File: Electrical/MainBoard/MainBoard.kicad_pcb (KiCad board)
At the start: 4 copper layers, 100 x 86.3 mm, 137 parts, among them J1 SNAP Program, J13 Refl_PCB_Connect, J14 Refl_PCB_Connect, J15 Refl_PCB_Connect, J16 Conn_02x03_Odd_Even, J17 MEM2061-01-188-00-A, J18 Conn_02x02_Odd_Even, J19 Conn_02x03_Odd_Even, J2 3.3V Supply, J20 Conn_01x06, J21 Conn_02x03_Odd_Even, J22 Conn_02x02_Odd_Even, J23 Conn_02x03_Odd_Even, J24 Conn_01x04, J25 Conn_02x02_Odd_Even, J26 Conn_02x04_Odd_Even, J3 5V Supply, J4 USB_B_Micro, J5 Battery1, J6 Battery1, J7 GPIO1, J8 Conn_02x04_Odd_Even, J9 USB_B_Micro, SW1 Reset, SW10 SW_SPST, SW2 5V Bypass, SW3 All Power Switch, SW4 User_Button, SW5 User_Button, SW6 User_Button, SW7 SW_SPST, SW8 SW_SPST, SW9 SW_SPST, U1 PIC32MZ2048EFH144-I/PL, U10 DRV8842PWPR, U11 Quad_Encoder_Motor, U12 Quad_Encoder_Motor, U13 DRV8842PWPR, U15 M95M01-DFMN6TP, U2 AP2114HA-3.3TRG1, U3 AP2114HA-3.3TRG1, U5 GSF7002DW, U6 GSF7002DW, U7 GSF7002DW, U8 GSF7002DW, U9 MCP2221A-I_SL

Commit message: Finalize main board and bom
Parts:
- moved C28 6.23 mm to (256.9, 128.2)
- moved U11 6.23 mm to (261.8, 121.8)
- moved U9 5.60 mm to (258.2, 109.3)
- moved C19 5.60 mm to (260.1, 115.0)
- moved D10 5.60 mm to (264.4, 114.1)
- moved D9 5.60 mm to (264.4, 107.6)
- moved J9 5.60 mm to (263.9, 100.0)
- moved R15 5.60 mm to (256.4, 97.0)
- moved R16 5.60 mm to (256.4, 99.1)
- moved J5 0.11 mm to (250.0, 101.0)
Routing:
- net Vdrive: track 208.4 -> 199.3 mm
- net Net-(U11-M-): track 18.3 -> 12.2 mm
- net Net-(U11-M+): track 21.5 -> 16.1 mm
- net /IC2: track 43.6 -> 41.1 mm
- net /IC1: track 39.5 -> 37.1 mm
- net /U1TX: track 49.4 -> 47.0 mm
- net /USB_RST: track 53.7 -> 51.3 mm
- net /U1RX: track 56.7 -> 56.0 mm
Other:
- board text added: "NiMH Batt."

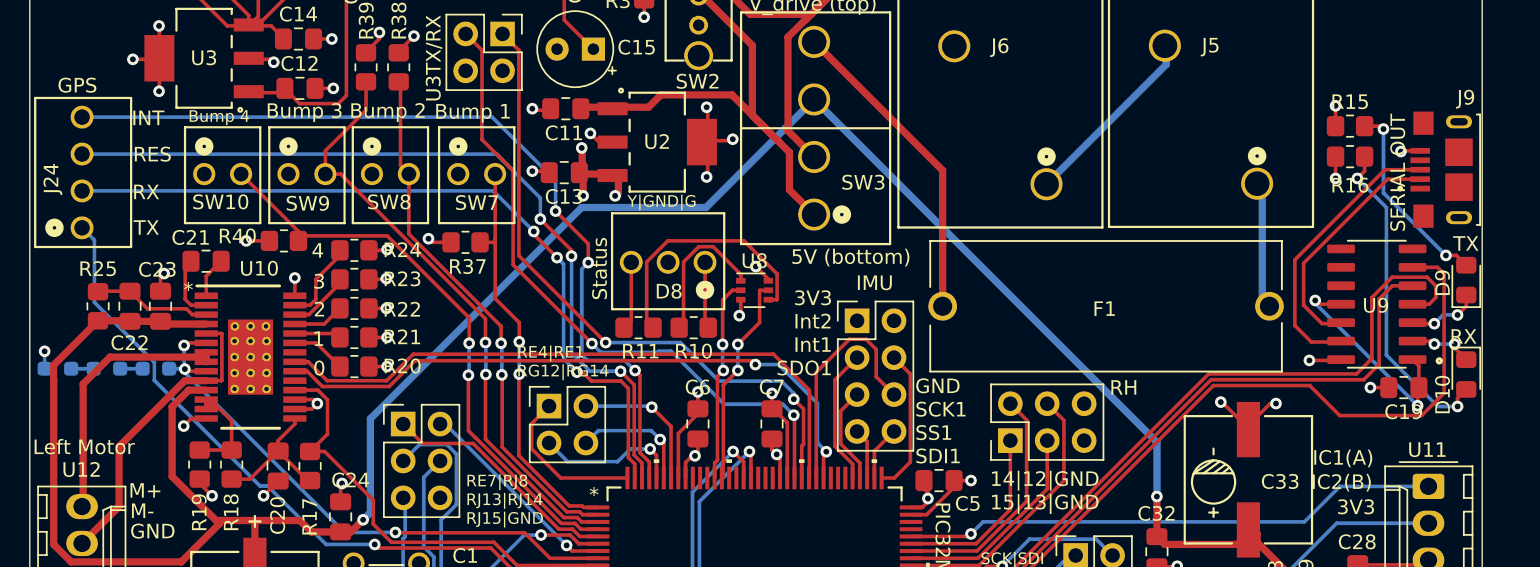
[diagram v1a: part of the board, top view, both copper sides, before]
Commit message: Update the status LED to common anode
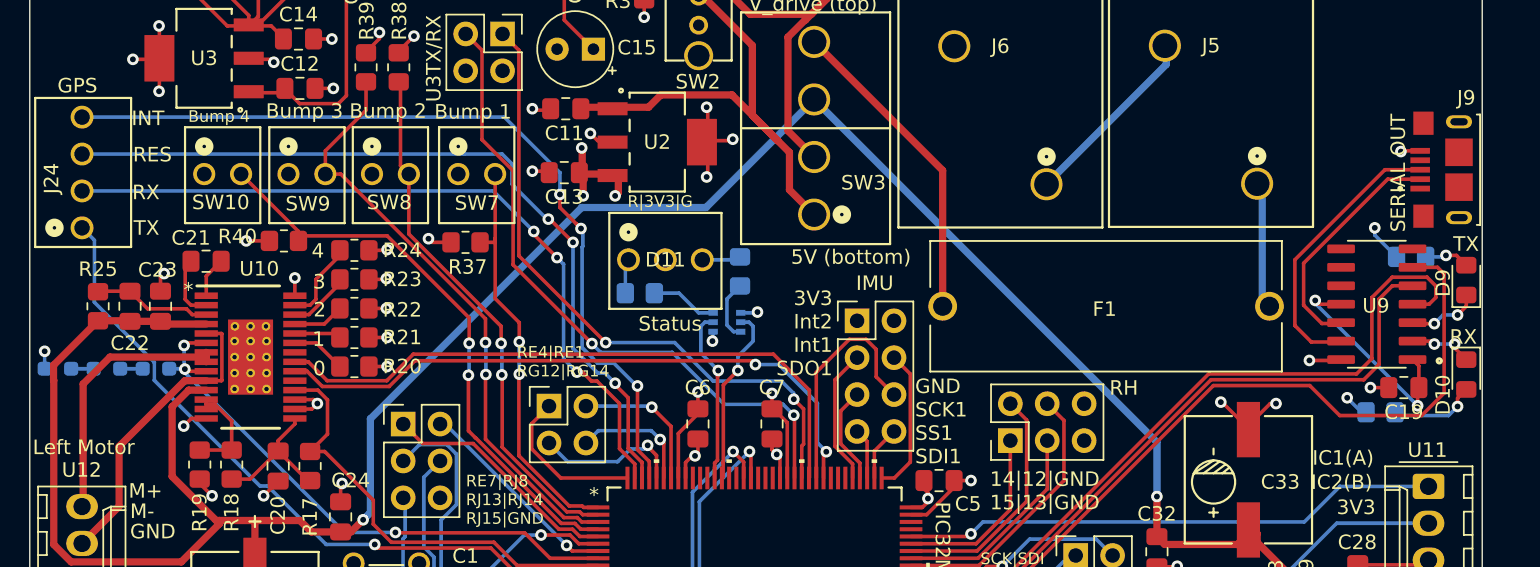
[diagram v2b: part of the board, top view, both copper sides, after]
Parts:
- removed D8: Status_LED, RobotLibrary:CONN3_22232031_MOL
- added D11: Status_LED, RobotLibrary:CONN3_22232031_MOL, F.Cu at (206.7, 106.2)
- R10, R11, R15, R16, U8: moved to B.Cu
- moved R16 17.7 mm to (258.5, 116.7)
- moved R15 9.93 mm to (260.6, 106.0)
- moved R10 5.02 mm to (214.4, 107.0), turned to 90 degrees
- moved U8 2.91 mm to (213.5, 110.5)
- moved R11 2.38 mm to (207.5, 108.5), turned to 180 degrees
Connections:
- R10 pad 1: Net-(D8-A1) -> Net-(U8-D1)
- R10 pad 2: Net-(U8-S1) -> Net-(D11-K2)
- R11 pad 1: Net-(D8-A2) -> Net-(U8-D2)
- R11 pad 2: Net-(U8-S2) -> Net-(D11-K1)
- U8 pad 1: Net-(U8-S1) -> GND
- U8 pad 3: +3.3V -> Net-(U8-D2)
- U8 pad 4: Net-(U8-S2) -> GND
- U8 pad 6: +3.3V -> Net-(U8-D1)
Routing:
- net Net-(U8-S2): track 17.0 -> 0.00 mm
- net Net-(D10-A): track 22.5 -> 6.08 mm, vias 2 -> 1
- net Net-(D9-A): track 13.5 -> 3.12 mm, vias 2 -> 1
- net Net-(U8-S1): track 9.83 -> 0.00 mm
- net Net-(D8-A2): track 4.71 -> 0.00 mm
- net Net-(U8-D2): track 0.00 -> 4.61 mm
- net Net-(D8-A1): track 4.28 -> 0.00 mm
- net Net-(U8-D1): track 0.00 -> 4.04 mm
- net Net-(D11-K2): track 0.00 -> 3.65 mm
- net Net-(D11-K1): track 0.00 -> 2.83 mm
- net /Status_Yellow: track 14.6 -> 12.3 mm, vias 2 -> 1
- net /Status_Green: track 14.0 -> 12.2 mm, vias 2 -> 1
- net GND: track 138.2 -> 140.1 mm, vias 66 -> 68
- net +3.3V: track 148.3 -> 147.3 mm, vias 40 -> 38
- net /U2RX: track 53.5 -> 52.6 mm
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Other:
- board text added: "R|3V3|G"
- board text removed: "Y|GND|G"

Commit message: Finalize the PCBs
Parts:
- moved C24 1.10 mm to (186.9, 122.8)
- moved C1 0.65 mm to (196.1, 128.2)
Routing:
- net /USB_RST: track 51.3 -> 45.0 mm, vias 0 -> 2
- net Net-(D10-K): track 4.39 -> 5.30 mm
- net /Fault1: track 30.6 -> 31.5 mm
- net Vdrive: track 199.3 -> 198.5 mm
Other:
- board text added: "Matthew Sato, 06/11/2025 Engineering Informatics Group Stanford University Robot Control Board, Rev 0.3 Schematic Details: https://github.com/satomm1/Robot"
- board text removed: "Matthew Sato, 05/18/2025 Engineering Informatics Group Stanford University Robot Control Board, Rev 0.3 Schematic Details: https://github.com/satomm1/Robot"

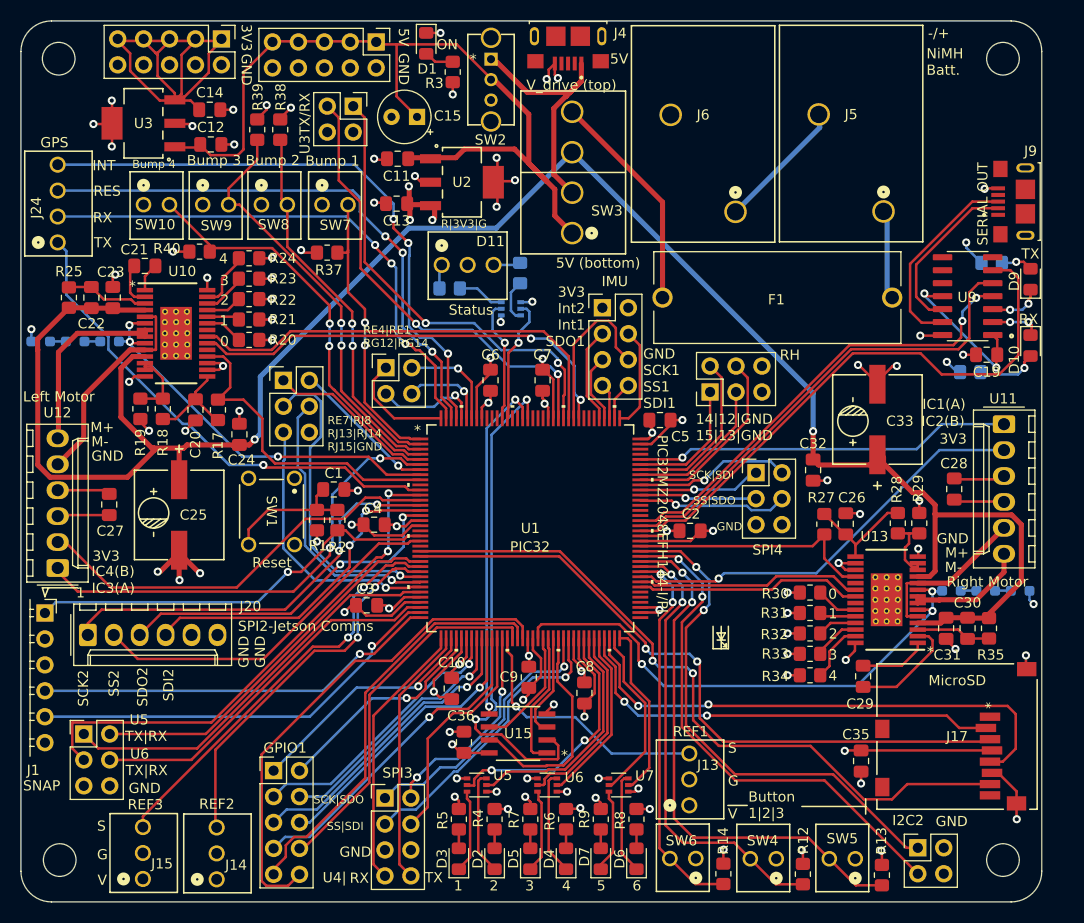
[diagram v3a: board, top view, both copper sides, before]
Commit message: Change some connections to picoblade, add env sensor connector
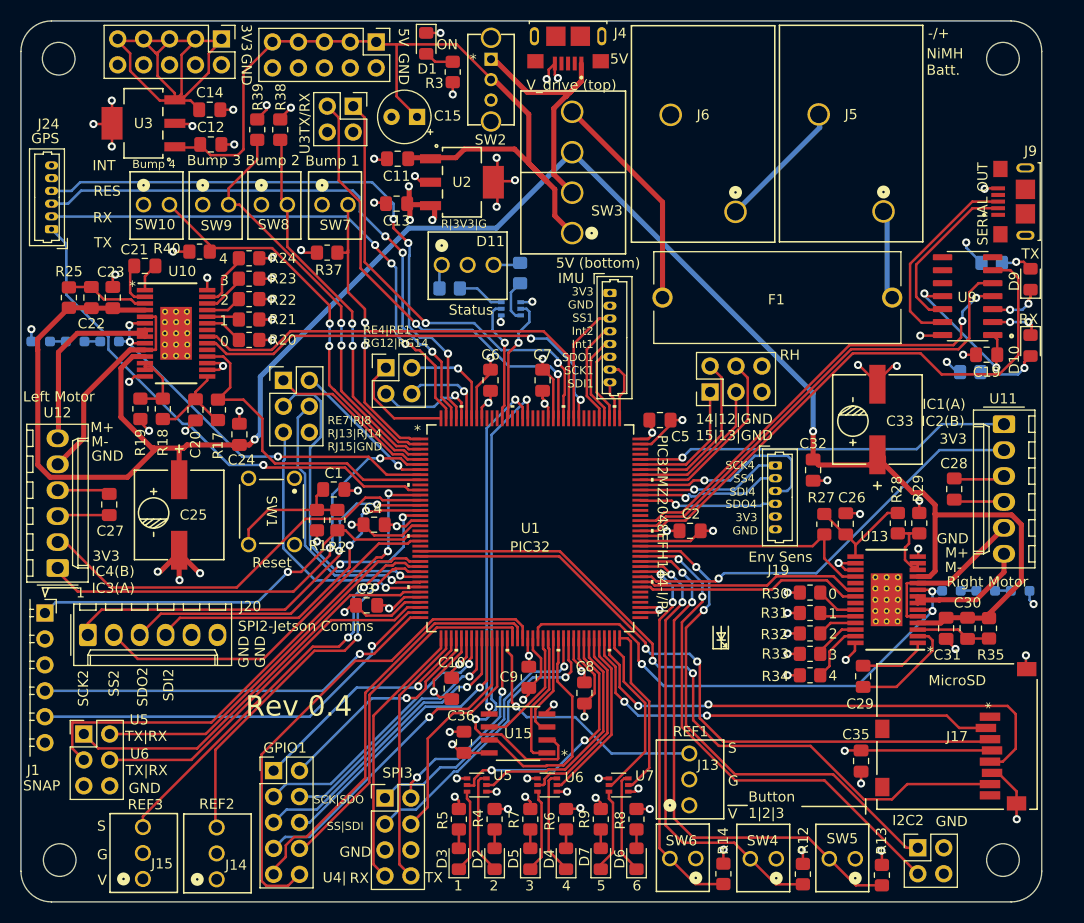
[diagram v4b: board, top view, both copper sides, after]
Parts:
- removed J26: Conn_02x04_Odd_Even, Connector_PinHeader_2.54mm:PinHeader_2x04_P2.54mm_Vertical
- added J30: Conn_01x08, Connector_Molex:Molex_PicoBlade_53047-0810_1x08_P1.25mm_Vertical, F.Cu at (223.2, 109.0)
- J19: value Conn_02x03_Odd_Even -> Conn_01x06; footprint Connector_PinHeader_2.54mm:PinHeader_2x03_P2.54mm_Vertical -> Connector_Molex:Molex_PicoBlade_53047-0610_1x06_P1.25mm_Vertical
- J24: value Conn_01x04 -> Conn_01x06; footprint RobotLibrary:CONN_22-23-2041_MOL -> Connector_Molex:Molex_PicoBlade_53047-0610_1x06_P1.25mm_Vertical
- moved J19 2.02 mm to (239.4, 125.8), turned to -90 degrees
- moved J24 1.43 mm to (168.5, 102.7)
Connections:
- J19 pad 2: /SDI4 -> /SS4*
- J19 pad 3: /SS4* -> /SDI4
- J19 pad 5: GND -> +3.3V
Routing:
- net /SDI4: track 15.3 -> 20.6 mm
- net /SS1*: track 16.2 -> 11.9 mm
- net /SDO1: track 3.49 -> 7.55 mm
- net /SCK1: track 10.1 -> 6.04 mm
- net /SS4*: track 11.5 -> 14.3 mm
- net /SCK4: track 11.6 -> 14.2 mm
- net /IMU_INT1: track 6.75 -> 8.40 mm
- net /U2TX: track 48.8 -> 50.4 mm
- net Net-(D11-K2): track 3.65 -> 2.40 mm
- net /SDO4: track 14.7 -> 13.5 mm
- net /GPS_Reset: track 55.9 -> 56.8 mm
- net Net-(D11-K1): track 2.83 -> 2.08 mm
- net /U2RX: track 52.6 -> 53.1 mm
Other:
- board text added: "3V3 GND SS1 Int2 Int1 SDO1 SCK1 SDI1"
- board text added: "Env Sens"
- board text added: "Matthew Sato, 08/04/2025 Engineering Informatics Group Stanford University Robot Control Board, Rev 0.4 Schematic Details: https://github.com/satomm1/Robot"
- board text added: "Rev 0.4"
- board text added: "SCK4"
- board text added: "SDI4"
- board text added: "SDO4"
- board text added: "SS4"
- board text removed: "3V3 Int2 Int1 SDO1"
- board text removed: "GND SCK1 SS1 SDI1"
- board text removed: "Matthew Sato, 06/11/2025 Engineering Informatics Group Stanford University Robot Control Board, Rev 0.3 Schematic Details: https://github.com/satomm1/Robot"
- board text removed: "SCK|SDI"
- board text removed: "SPI4"
- board text removed: "SS|SDO"

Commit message: Use more molex picoblades and make schematic prettier
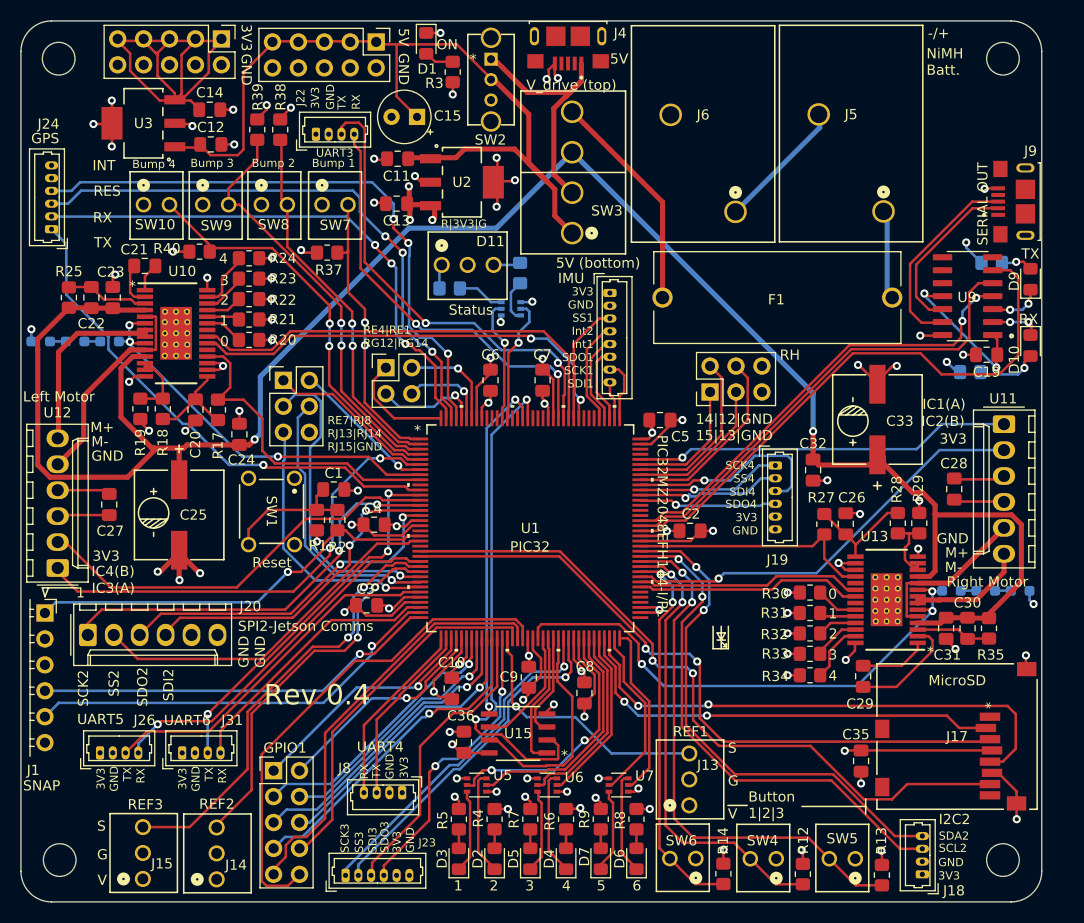
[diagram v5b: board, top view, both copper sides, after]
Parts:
- added J26: Conn_01x04, Connector_Molex:Molex_PicoBlade_53047-0410_1x04_P1.25mm_Vertical, F.Cu at (173.2, 154.0)
- added J31: Conn_01x04, Connector_Molex:Molex_PicoBlade_53047-0410_1x04_P1.25mm_Vertical, F.Cu at (181.3, 154.0)
- J18, J22: value Conn_02x02_Odd_Even -> Conn_01x04; footprint Connector_PinHeader_2.54mm:PinHeader_2x02_P2.54mm_Vertical -> Connector_Molex:Molex_PicoBlade_53047-0410_1x04_P1.25mm_Vertical
- J23: value Conn_02x03_Odd_Even -> Conn_01x06; footprint Connector_PinHeader_2.54mm:PinHeader_2x03_P2.54mm_Vertical -> Connector_Molex:Molex_PicoBlade_53047-0610_1x06_P1.25mm_Vertical
- J8: value Conn_02x04_Odd_Even -> Conn_01x04; footprint Connector_PinHeader_2.54mm:PinHeader_2x04_P2.54mm_Vertical -> Connector_Molex:Molex_PicoBlade_53047-0410_1x04_P1.25mm_Vertical
- moved J23 29.1 mm to (197.3, 166.0)
- moved J22 4.57 mm to (194.4, 93.4), turned to 0 degrees
- moved J18 2.64 mm to (253.8, 165.9), turned to 90 degrees
- moved J8 1.77 mm to (202.8, 157.9), turned to 180 degrees
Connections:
- J18 pad 1: /SDA2 -> +3.3V
- J18 pad 4: GND -> /SDA2
- J22 pad 1: /U3TX -> +3.3V
- J22 pad 3: /U3RX -> /U3TX
- J22 pad 4: GND -> /U3RX
- J23 pad 1: /U5TX -> /SCK3
- J23 pad 2: /U5RX -> /SS3*
- J23 pad 3: /U6TX -> /SDI3
- J23 pad 4: /U6RX -> /SDO3
- J23 pad 5: GND -> +3.3V
- J8 pad 1: /SCK3 -> +3.3V
- J8 pad 2: /SDO3 -> GND
- J8 pad 3: /SS3* -> /U4TX
- J8 pad 4: /SDI3 -> /U4RX
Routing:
- net /U6TX: track 50.9 -> 36.9 mm, vias 2 -> 3
- net /U6RX: track 36.6 -> 26.7 mm
- net /SDO3: track 20.6 -> 28.9 mm
- net /U4RX: track 26.5 -> 18.3 mm
- net /SCK3: track 26.8 -> 34.2 mm
- net /U4TX: track 25.6 -> 18.3 mm
- net /SDI3: track 22.7 -> 29.2 mm
- net /SS3*: track 28.9 -> 34.2 mm
- net /U5TX: track 39.9 -> 35.4 mm
- net /U3RX: track 45.2 -> 41.4 mm
- net /Refl3: track 40.7 -> 43.3 mm
- net /U5RX: track 37.7 -> 36.2 mm, vias 0 -> 1
- net /U3TX: track 44.7 -> 45.5 mm
- net /SCL2: track 51.2 -> 50.6 mm
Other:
- board text added: "Matthew Sato, 08/08/2025 Engineering Informatics Group Stanford University Robot Control Board, Rev 0.4 Schematic Details: https://github.com/satomm1/Robot"
- board text added: "SCK3"
- board text added: "SCL2"
- board text added: "SDA2"
- board text added: "SDI3"
- board text added: "SDO3"
- board text added: "SS3"
- board text added: "UART3"
- board text added: "UART4"
- board text added: "UART5"
- board text added: "UART6"
- board text removed: "Env Sens"
- board text removed: "Matthew Sato, 08/04/2025 Engineering Informatics Group Stanford University Robot Control Board, Rev 0.4 Schematic Details: https://github.com/satomm1/Robot"
- board text removed: "SCK|SDO"
- board text removed: "SPI3"
- board text removed: "SS|SDI"
- board text removed: "U3TX/RX"
- board text removed: "U4|"
- board text removed: "U5 TX|RX"
- board text removed: "U6 TX|RX"

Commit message: Finalize updated schematics
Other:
- board text added: "Env. Sens"
- board text removed: "I2C2"
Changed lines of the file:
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@@
 		(sheetname "/SPI_UART/")
 		(sheetfile "SPI_UART.kicad_sch")
-		(attr through_hole)
+		(attr through_hole exclude_from_bom)
 		(fp_line
 			(start -1.9 1.55)
@@
 		(sheetname "/Memory/")
 		(sheetfile "Memory.kicad_sch")
-		(attr smd)
+		(attr smd exclude_from_bom)
 		(fp_line
 			(start -0.261252 0.735)
@@
 		(sheetname "/SPI_UART/")
 		(sheetfile "SPI_UART.kicad_sch")
-		(attr through_hole)
+		(attr through_hole exclude_from_bom)
 		(fp_line
 			(start -1.9 1.55)
@@
 		(sheetname "/Buttons/")
 		(sheetfile "Buttons.kicad_sch")
-		(attr smd exclude_from_bom)
+		(attr smd)
 		(fp_line
 			(start -0.227064 -0.735)
@@
 		(sheetname "/SPI_UART/")
 		(sheetfile "SPI_UART.kicad_sch")
-		(attr through_hole)
+		(attr through_hole exclude_from_bom)
 		(fp_line
 			(start -1.9 1.55)
@@
 		(sheetname "/SPI_UART/")
 		(sheetfile "SPI_UART.kicad_sch")
-		(attr through_hole)
+		(attr through_hole exclude_from_bom)
 		(fp_line
 			(start -1.9 1.55)
@@
 		(sheetname "/SPI_UART/")
 		(sheetfile "SPI_UART.kicad_sch")
-		(attr through_hole)
+		(attr through_hole exclude_from_bom)
 		(fp_line
 			(start 5.36 1.26)
@@
 		(sheetname "/Memory/")
 		(sheetfile "Memory.kicad_sch")
-		(attr smd)
+		(attr smd exclude_from_bom)
 		(fp_line
 			(start 2.1209 -2.6289)
@@
 		(sheetname "/Buttons/")
 		(sheetfile "Buttons.kicad_sch")
-		(attr smd exclude_from_bom)
+		(attr smd)
 		(fp_line
 			(start -0.227064 -0.735)
@@
 		(sheetname "/Buttons/")
 		(sheetfile "Buttons.kicad_sch")
-		(attr through_hole exclude_from_bom)
+		(attr through_hole)
 		(fp_line
 			(start 3.8608 3.3782)
@@
 		(sheetname "/Buttons/")
 		(sheetfile "Buttons.kicad_sch")
-		(attr through_hole exclude_from_bom)
+		(attr through_hole)
 		(fp_line
 			(start 3.8608 3.3782)
@@
 		(sheetname "/Memory/")
 		(sheetfile "Memory.kicad_sch")
-		(attr smd)
+		(attr smd exclude_from_bom)
 		(fp_line
 			(start -0.261252 -0.735)
@@
 		(sheetname "/GPS/")
 		(sheetfile "GPS.kicad_sch")
-		(attr through_hole)
+		(attr through_hole exclude_from_bom)
 		(fp_line
 			(start 7.86 -2.16)
@@
 		(sheetname "/Memory/")
 		(sheetfile "Memory.kicad_sch")
-		(attr smd)
+		(attr smd exclude_from_bom)
 		(fp_line
 			(start 7.1247 -7.8486)
@@
 		(sheetname "/SPI_UART/")
 		(sheetfile "SPI_UART.kicad_sch")
-		(attr through_hole)
+		(attr through_hole exclude_from_bom)
 		(fp_line
 			(start -1.9 1.55)
@@
 	)
 	(gr_line
-		(start 263.3875 136.01125)
-		(end 263.3875 137.58875)
+		(start 263.642224 140.21125)
+		(end 263.642224 141.78875)
 		(stroke
 			(width 0.15)
@@
 		)
 	)
-	(gr_text "I2C2"
+	(gr_text "Env. Sens"
 		(at 255.4 161.1 0)
 		(layer "F.SilkS")
@@
 	)
 	(gr_text "0.05R"
-		(at 265 135.9 0)
+		(at 264.7 143.1 0)
 		(layer "B.SilkS")
 		(effects
